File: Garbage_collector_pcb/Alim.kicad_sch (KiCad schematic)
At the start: 0 parts

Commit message: Ajout de la partie alimentation
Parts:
- added BT1: Battery_Cell, symbol Kicad:Battery_Cell
- added C12, C13: 10µF, symbol Kicad:C
- added C14, C17: 47nF, symbol Kicad:C
- added C18: 1µF, symbol Kicad:C
- added C19: 8µ2, symbol Kicad:C
- added J11: USB_C_Receptacle_USB2.0_16P, Connector_USB:USB_C_Receptacle_GCT_USB4105-xx-A_16P_TopMnt_Horizontal, symbol Kicad:USB_C_Receptacle_USB2.0_16P
- added L1: L, symbol Kicad:L
- added Q1: NMOS, symbol Kicad:NMOS
- added R10: 260, symbol Kicad:R
- added R11, R12, R13, R14, R16, R19: 10k, symbol Kicad:R
- added R15: 1k, symbol Kicad:R
- added R17: 5k23, symbol Kicad:R
- added R18: 30k1, symbol Kicad:R
- added R7, R8: 5.1k, Resistor_SMD:R_0402_1005Metric_Pad0.72x0.64mm_HandSolder, symbol Device:R
- added SW1: SW_Push, symbol Kicad:SW_Push
- added U2: BQ25896RTWR, Package_DFN_QFN:Texas_RTW_WQFN-24-1EP_4x4mm_P0.5mm_EP2.7x2.7mm, symbol Ext_library:BQ25896RTWR
- added U4: USBLC6-2P6, Package_TO_SOT_SMD:SOT-23-6, symbol Power_Protection:USBLC6-2P6
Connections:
- new net: R10.2, U2.10 (ILIM)
- new net: R17.2, R18.1, R19.1, U2.11 (TS)
- new net: SW1.1, U2.12 (~{QON})
- new net: BT1.1 (+), U2.13 (BAT), U2.14 (BAT)
- new net: C14.2, L1.1, U2.19 (SW), U2.20 (SW)
- new net: C12.1, C13.1, C14.1, U2.21 (BTST)
- new net: C19.2, U2.23 (PMID)
- new net: J11.A5 (CC1), R7.1
- new net: J11.B5 (CC2), R8.2
- new net: Q1.2 (G), R14.2, R15.2
- new net +3.3V: R11.1, R12.2, R13.1
- new net D+: J11.A6 (D+), J11.B6 (D+), U4.3 (I/O2)
- new net D-: J11.A7 (D-), J11.B7 (D-), U4.1 (I/O1)
- new net DP+: U4.4 (I/O2)
- new net DP-: U4.6 (I/O1)
- new net EXP: BT1.2 (-), C17.1, C18.1, C19.1, J11.A1 (GND), J11.A12 (GND), J11.B1 (GND), J11.B12 (GND), J11.SH (SHIELD), Q1.3 (S), R10.1, R14.1, R18.2, R19.2, R7.2, R8.1, SW1.2, U2.17 (PGND), U2.18 (PGND), U2.2 (PSEL), U2.25 (EXP), U2.9 (~{CE}), U4.2 (GND)
- new net INT: R11.2, U2.7 (INT)
- new net OTG: Q1.1 (D), R16.1, U2.8 (OTG)
- new net REGN: C17.2, R17.1, U2.22 (REGN)
- new net SCL: U2.5 (SCL)
- new net SDA: U2.6 (SDA)
- new net STAT: R12.1, U2.4 (STAT)
- new net SYS: C12.2, C13.2, L1.2, R16.2, U2.15 (SYS), U2.16 (SYS)
- new net VBUS: C18.2, J11.A4 (VBUS), J11.A9 (VBUS), J11.B4 (VBUS), J11.B9 (VBUS), R15.1, U2.1 (VBUS), U4.5 (VBUS)
- new net ~{PG}: R13.2, U2.3 (~{PG})
- no-connect marks 0 -> 2
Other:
- note added: "Activation du boost interne (Si USB absent)"
- note added: "Chargeur"
- note added: "Connecteur USB C"
- note added: "Protection ESD"
- note added: "Resistances de tirage"

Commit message: update alim part
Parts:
- removed J11: USB_C_Receptacle_USB2.0_16P, Connector_USB:USB_C_Receptacle_GCT_USB4105-xx-A_16P_TopMnt_Horizontal, symbol Kicad:USB_C_Receptacle_USB2.0_16P
- removed U4: USBLC6-2P6, Package_TO_SOT_SMD:SOT-23-6, symbol Power_Protection:USBLC6-2P6
- added C20, C21: 10µ, symbol Kicad:C
- added C22: 470nF, symbol Kicad:C
- added C23: 2µ2, symbol Kicad:C
- added J12: USB_C_Receptacle_PowerOnly_6P, symbol Kicad:USB_C_Receptacle_PowerOnly_6P
- added PS1: BU33SD5WG-TR, BU33SD5WG-TR:SOT95P280X125-5N, symbol Kicad:BU33SD5WG-TR
- added R20, R21: 10k, symbol Kicad:R
- added R9: 10m, Resistor_SMD:R_0402_1005Metric_Pad0.72x0.64mm_HandSolder, symbol Device:R
- added U4: BQ27220YZFR, YZF9_TEX, symbol Ext_library:BQ27220YZFR
- C17: value 47nF -> 4µ7
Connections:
- net +3.3V: now also R20.1
- net EXP: now also C12.1, C13.1, C20.1, C21.1, C22.1, C23.1, J12.A12 (GND), J12.B12 (GND), J12.SH (SHIELD), PS1.2 (GND), R21.2, U4.B2 (VSS)
- net VBUS: now also J12.A9 (VBUS), J12.B9 (VBUS), PS1.1 (VIN), PS1.3 (STBY)
- net +BATT: now reaches U2.13 (BAT), U2.14 (BAT)
- net +BATT: now also R9.1, U4.C2 (SRN); no longer BT1.1 (+)
- net at C14.1, U2.21 (BTST): no longer C12.1, C13.1
- net at R7.1: now also J12.A5 (CC1)
- net at R8.2: now also J12.B5 (CC2)
- new net: R21.1, U4.B1 (VIN)
- new net: R20.2, U4.A1 (GPOUT)
- new net: C22.2, C23.2, U4.B3 (VDD)
- new net: C21.2, PS1.5 (VOUT)
- new net BAT+: BT1.1 (+), R9.2, U4.C1 (SRP)
- no-connect marks 2 -> 0
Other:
- note removed: "Protection ESD"
- moved on the sheet: Q1, R11, R12, R13, R14, R15, R16, R7, R8

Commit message: update alim part
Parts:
- added C24: 1µF, symbol Kicad:C
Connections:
- net SCL is gone; now on net I2C1_SCL: U2.5 (SCL)
- net SDA is gone; now on net I2C1_SDA: U2.6 (SDA)
- net EXP: now also C24.1
- net I2C1_SDA: now reaches U4.A2 (SDA)
- net I2C1_SCL: now reaches U4.A3 (SCL)
- net BAT+ renamed bat
- net bat: now also U4.C3 (BAT), C24.2
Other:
- note added: "Batterie - Lipo 1S 3400mAh"
- moved on the sheet: BT1, C12, C13, C14, C17, C18, C19, C22, C23, L1, Q1, R10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

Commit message: seance 24 septembre
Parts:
- added D3: D, symbol Kicad:D
- added Q4: MMDT5401, Package_TO_SOT_SMD:SOT-363_SC-70-6, symbol Kicad:MMDT5401
- added Q5: PMOS, symbol Kicad:PMOS
- added R22, R23: 100k, symbol Kicad:R
- PS1: footprint BU33SD5WG-TR:SOT95P280X125-5N -> Package_SO:TSOP-5_1.65x3.05mm_P0.95mm
- U4: footprint YZF9_TEX -> Package_BGA:Texas_DSBGA-9_1.4715x1.4715mm_Layout3x3_P0.5mm
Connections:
- net +3.3V: now also C21.2, PS1.5 (VOUT)
- net +BATT: now also C20.2, PS1.1 (VIN), PS1.3 (STBY)
- net EXP: now also R22.1, R23.1
- net VBUS: now also D3.1 (K), Q4.4 (E2), Q5.1 (D); no longer PS1.1 (VIN), PS1.3 (STBY)
- net GPOUT: now reaches R20.2, U4.A1 (GPOUT)
- net I2C1_SCL renamed I2C3_SCL
- net I2C1_SDA renamed I2C3_SDA
- new net: D3.2 (A), Q4.2 (B1), Q4.3 (C2), Q4.5 (B2), R22.2
- new net: Q4.6 (C1), Q5.2 (G), R23.2
- new net USB_5V: Q4.1 (E1), Q5.3 (S)
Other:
- note added: "Fuel Gauge"

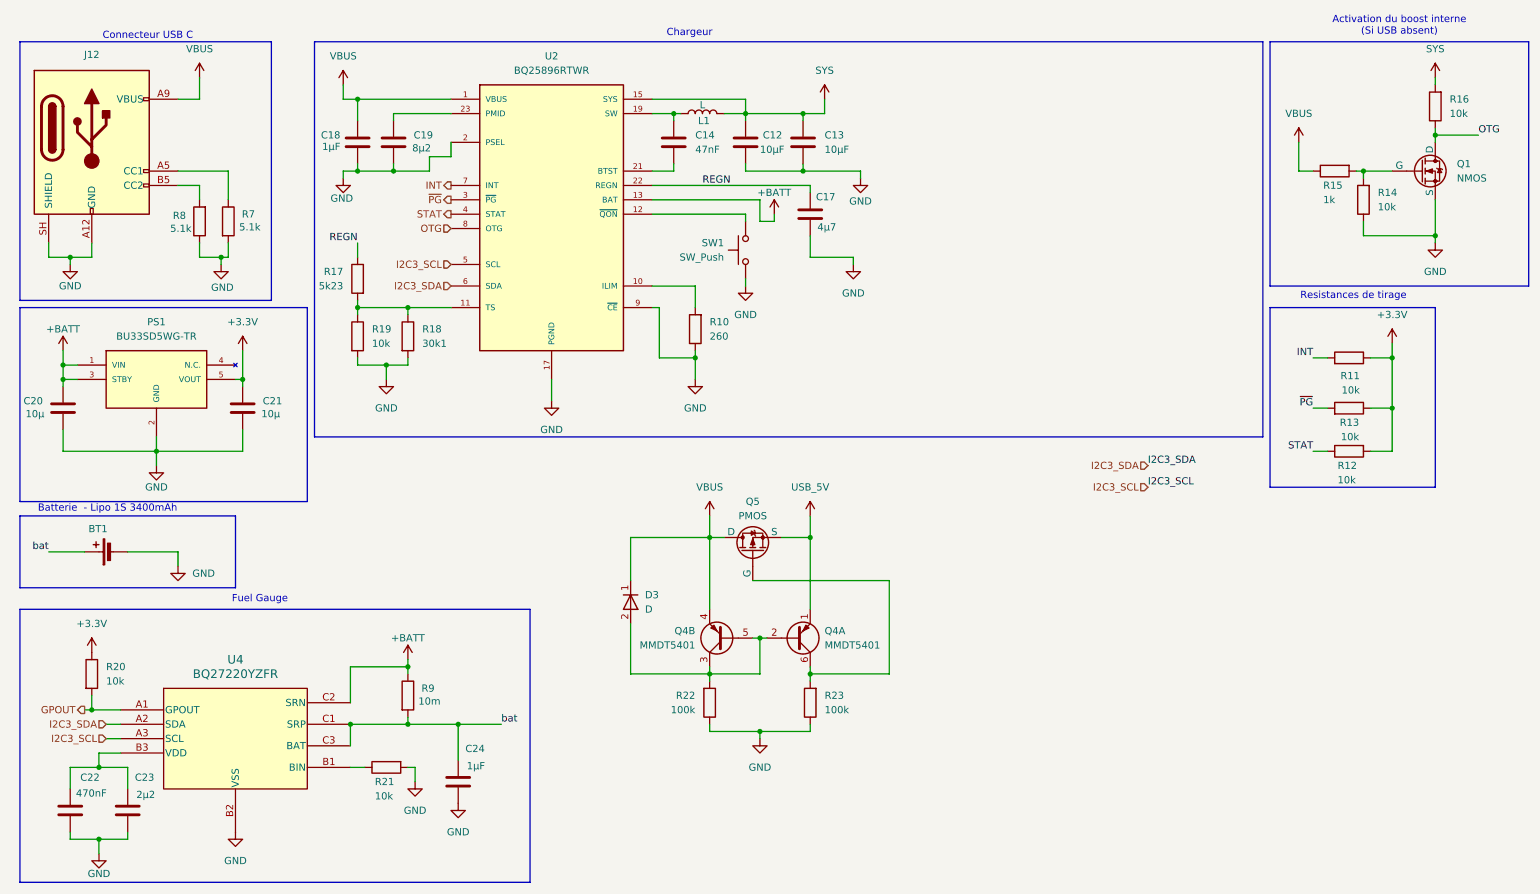
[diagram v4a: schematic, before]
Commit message: update schematic
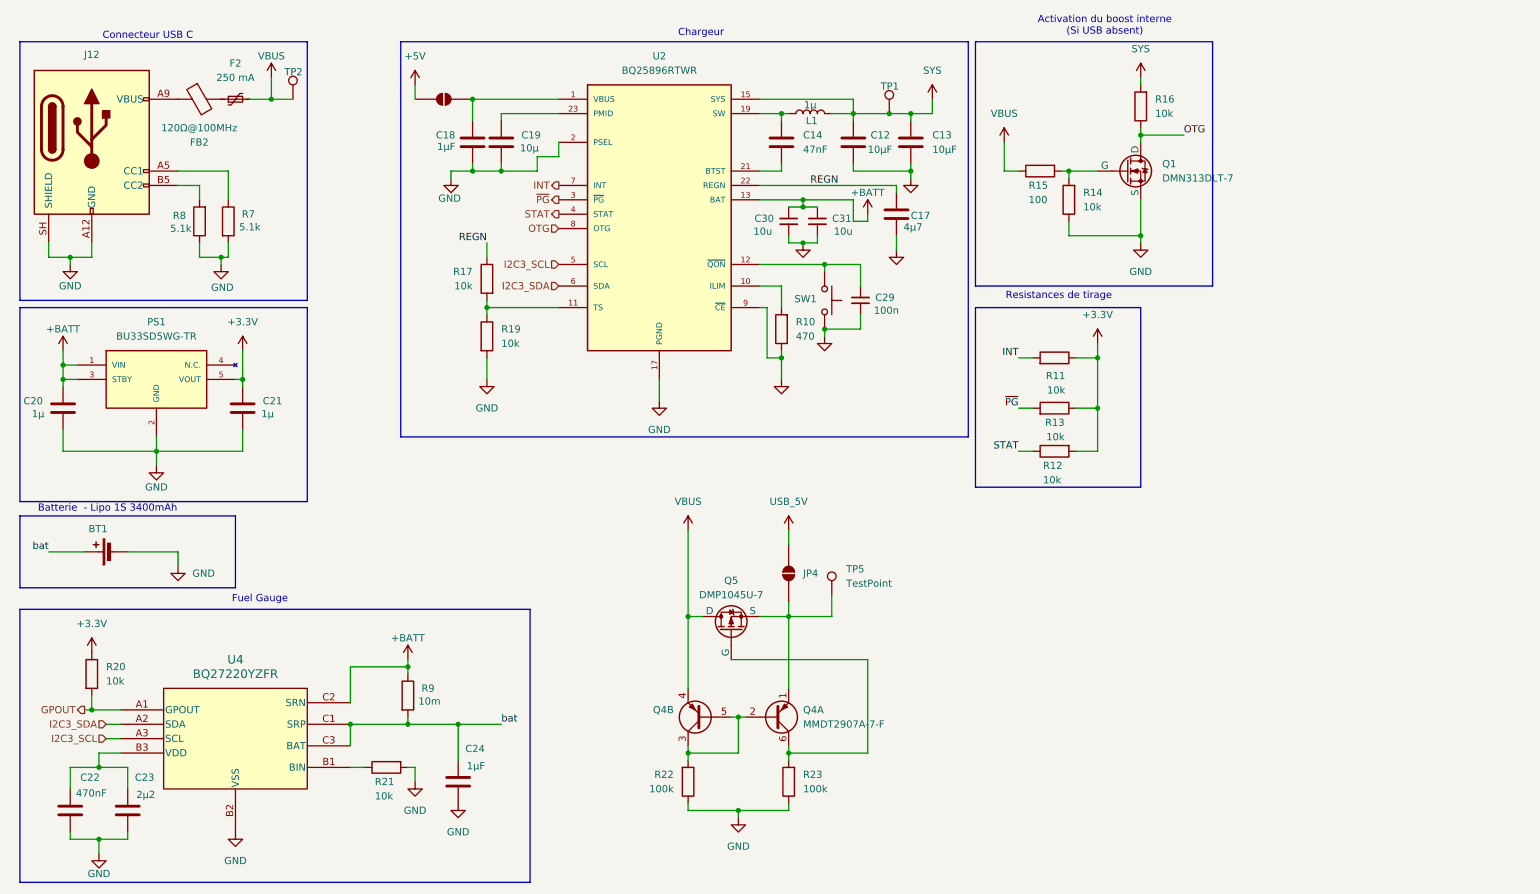
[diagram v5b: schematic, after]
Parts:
- removed D3: D, symbol Kicad:D
- removed R18: 30k1, symbol Kicad:R
- added C29: 100n, Capacitor_SMD:C_0402_1005Metric, symbol Device:C_Small
- added C30, C31: 10u, Capacitor_SMD:C_0402_1005Metric, symbol Device:C_Small
- added F2: 250 mA, Fuse:Fuse_0603_1608Metric, symbol Device:Polyfuse_Small
- added FB2: 120Ω@100MHz, Inductor_SMD:L_0603_1608Metric, symbol Device:FerriteBead
- added JP3, JP4: SolderJumper_2_Open, Jumper:SolderJumper-2_P1.3mm_Open_TrianglePad1.0x1.5mm, symbol Jumper:SolderJumper_2_Open
- added TP1, TP2, TP5: TestPoint, TestPoint:TestPoint_Pad_D2.0mm, symbol Connector:TestPoint
- C19: value 8µ2 -> 10µ
- C20, C21: value 10µ -> 1µ
- L1: value L -> 1µ
- Q1: value NMOS -> DMN313DLT-7
- Q4: value MMDT5401 -> MMDT2907A-7-F
- Q5: value PMOS -> DMP1045U-7; footprint (none) -> Package_TO_SOT_SMD:SOT-23
- R10: value 260 -> 470
- R15: value 1k -> 100
- R17: value 5k23 -> 10k
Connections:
- net +BATT: now also C30.1, C31.1
- net EXP: now also C29.2, C30.2, C31.2
- net SYS: now also TP1.1
- net USB_5V: now also JP4.2 (B); no longer Q4.1 (E1), Q5.3 (S)
- net VBUS: now also F2.2, TP2.1; no longer C18.2, J12.A9 (VBUS), J12.B9 (VBUS), U2.1 (VBUS)
- net at SW1.1, U2.12 (~{QON}): now also C29.1
- new net: F2.1, FB2.2
- new net: JP4.1 (A), Q4.1 (E1), Q5.3 (S), TP5.1
- new net: C18.2, JP3.2 (B), U2.1 (VBUS)
- new net: FB2.1, J12.A9 (VBUS), J12.B9 (VBUS)
- new net +5V: JP3.1 (A)
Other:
- moved on the sheet: C12, C13, C14, C17, C18, C19, L1, Q1, Q4A, Q4B, Q5, R10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

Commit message: ajout led temoin
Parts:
- added D3, D4, D5, D6: LED, symbol Kicad:LED
- added R24, R25: 1k5, Resistor_SMD:R_0402_1005Metric, symbol Device:R
- added R27, R28, R29, R30: 100k, symbol Kicad:R
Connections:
- net +3.3V: now also R24.1, R25.1, R27.2
- net +5V: now also R28.2
- net EXP: now also D3.1 (K), D4.1 (K)
- net I2C3_SCL: now also R25.2
- net I2C3_SDA: now also R24.2
- net STAT: now also D5.1 (K)
- net SYS: now also R29.2, R30.2
- net ~{PG}: now also D6.1 (K)
- new net: D4.2 (A), R28.1
- new net: D5.2 (A), R29.1
- new net: D6.2 (A), R30.1
- new net: D3.2 (A), R27.1

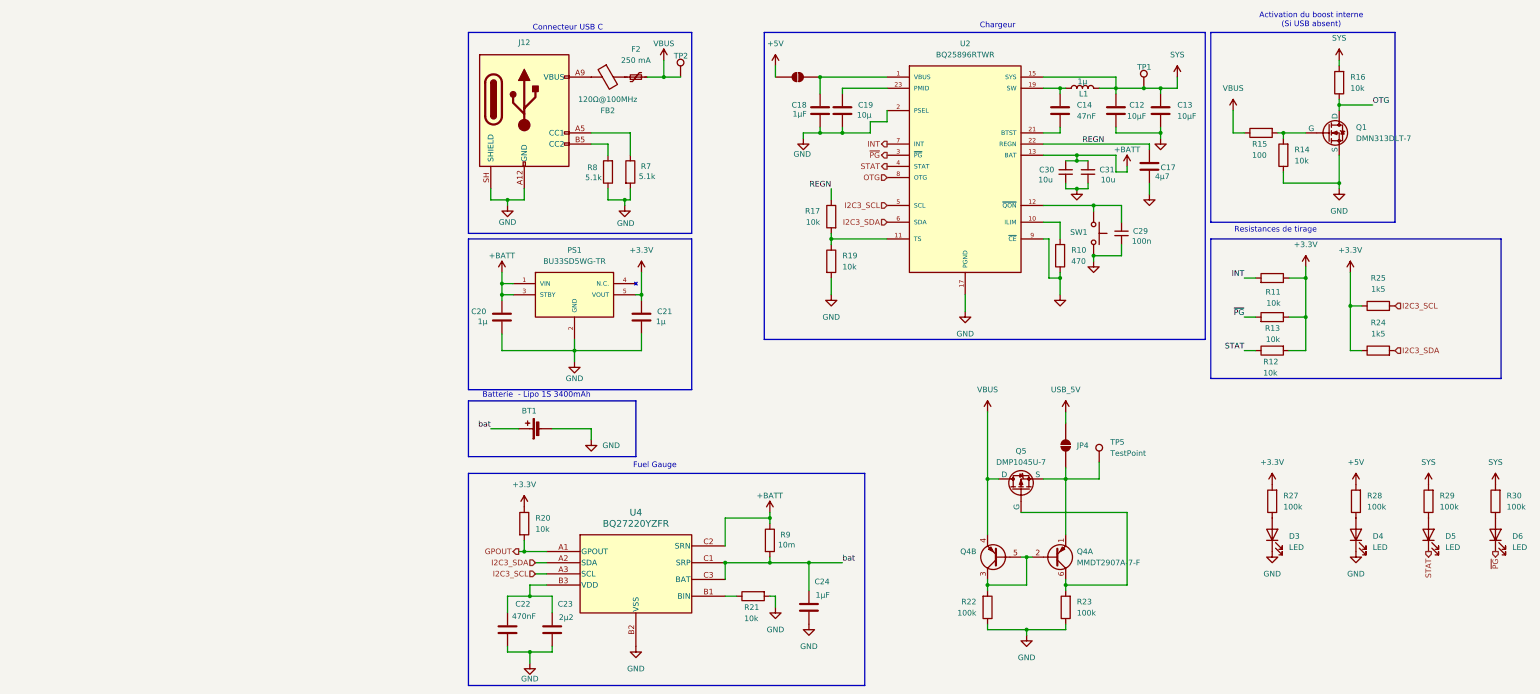
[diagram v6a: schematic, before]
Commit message: update schematic
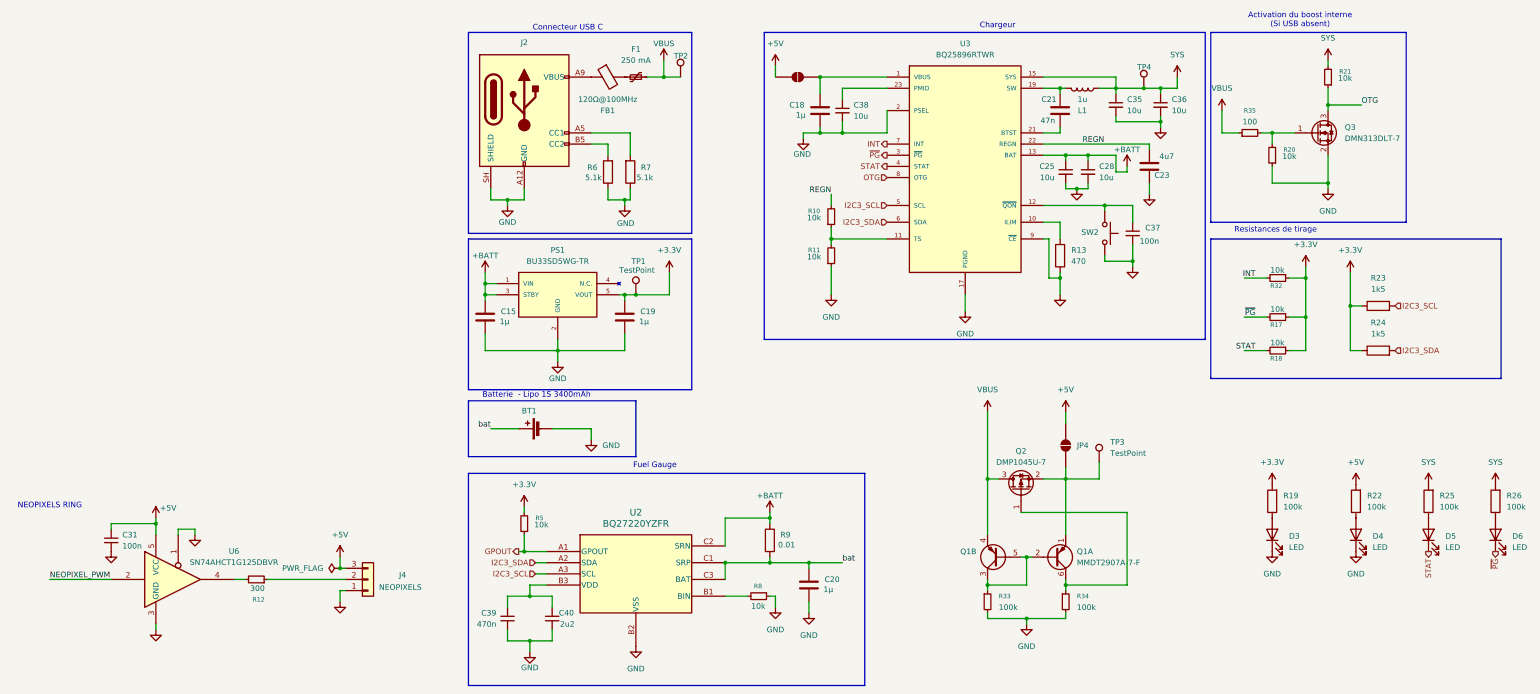
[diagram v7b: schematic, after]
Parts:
- removed C12, C13: 10µF, symbol Kicad:C
- removed C14: 47nF, symbol Kicad:C
- removed C17: 4µ7, symbol Kicad:C
- removed C21: 1µ, symbol Kicad:C
- removed C22: 470nF, symbol Kicad:C
- removed C23: 2µ2, symbol Kicad:C
- removed C24: 1µF, symbol Kicad:C
- removed C29: 100n, Capacitor_SMD:C_0402_1005Metric, symbol Device:C_Small
- removed C30: 10u, Capacitor_SMD:C_0402_1005Metric, symbol Device:C_Small
- removed L1: 1µ, symbol Kicad:L
- removed Q1: DMN313DLT-7, symbol Kicad:NMOS
- removed Q5: DMP1045U-7, Package_TO_SOT_SMD:SOT-23, symbol Kicad:PMOS
- removed R11, R12, R13, R14, R16, R17, R19, R20, R21: 10k, symbol Kicad:R
- removed R15: 100, symbol Kicad:R
- removed R22, R23: 100k, symbol Kicad:R
- added C20: 1µ, symbol Kicad:C
- added C21: 47n, Capacitor_SMD:C_0402_1005Metric, symbol Device:C
- added C23: 4u7, Capacitor_SMD:C_0402_1005Metric, symbol Device:C
- added C25, C28, C35, C36, C38: 10u, symbol Kicad:C_Small
- added C37: 100n, Capacitor_SMD:C_0402_1005Metric, symbol Device:C_Small
- added C39: 470n, Capacitor_SMD:C_0402_1005Metric, symbol Device:C_Small
- added C40: 2u2, Capacitor_SMD:C_0402_1005Metric, symbol Device:C_Small
- added J4: NEOPIXELS, Connector_JST:JST_GH_SM03B-GHS-TB_1x03-1MP_P1.25mm_Horizontal, symbol Connector_Generic:Conn_01x03
- added L1: 1u, Inductor_SMD:L_1008_2520Metric, symbol Device:L
- added Q2: DMP1045U-7, Package_TO_SOT_SMD:SOT-23, symbol Transistor_FET:DMP3099L
- added Q3: DMN313DLT-7, Package_TO_SOT_SMD:SOT-523, symbol Transistor_FET:DMN3150L
- added R10, R11, R17, R18, R20, R21, R32, R5, R8: 10k, Resistor_SMD:R_0402_1005Metric, symbol Device:R_Small
- added R12: 300, Resistor_SMD:R_0603_1608Metric, symbol Device:R_Small
- added R33, R34: 100k, Resistor_SMD:R_0402_1005Metric, symbol Device:R_Small
- added R35: 100, Resistor_SMD:R_0402_1005Metric, symbol Device:R_Small
- added TP1: TestPoint, TestPoint:TestPoint_Pad_D2.0mm, symbol Connector:TestPoint
- added U6: SN74AHCT1G125DBVR, Package_TO_SOT_SMD:SOT-23-5, symbol 74xGxx:74AHCT1G125
- BT1: JLCPCB Part # (none) -> C54769875
- C15: renamed from C20; JLCPCB Part # (none) -> C29266
- C18: value 1µF -> 1µ; JLCPCB Part # (none) -> C29266
- C19: value 10µ -> 1µ; JLCPCB Part # (none) -> C29266
- C31: value 10u -> 100n
- J2: renamed from J12; JLCPCB Part # (none) -> C2927026
- PS1: Availability In Stock -> (none); Check_prices https://www.snapeda.com/parts/BU33SD5WG-TR/Rohm/view-part/?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 -> (none); Description_1 Linear Voltage Regulator IC Positive Fixed 1 Output 500mA 5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 -> (none); HEIGHT 1.25mm -> (none); JLCPCB Part # (none) -> C3750265; MANUFACTURER_NAME ROHM Semiconductor -> (none); MANUFACTURER_PART_NUMBER BU33SD5WG-TR -> (none); MF Rohm -> (none); MOUSER_PART_NUMBER 755-BU33SD5WG-TR -> (none); MOUSER_PRICE-STOCK https://www.mouser.co.uk/ProductDetail/ROHM-Semiconductor/B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 -> (none); MP BU33SD5WG-TR -> (none); Package SSOP-5 Rohm -> (none); Price None -> (none); SnapEDA_Link https://www.snapeda.com/parts/BU33SD5WG-TR/Rohm/view-part/?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 -> (none)
- Q1: renamed from Q4; JLCPCB Part # (none) -> C460232
- R13: renamed from R10; JLCPCB Part # (none) -> C25117
- R6: renamed from R8; JLCPCB Part # (none) -> C25905
- R7: JLCPCB Part # (none) -> C25905
- R9: value 10m -> 0.01; footprint Resistor_SMD:R_0402_1005Metric_Pad0.72x0.64mm_HandSolder -> Resistor_SMD:R_2512_6332Metric; JLCPCB Part # (none) -> C105142
- SW2: renamed from SW1; JLCPCB Part# (none) -> C72443
- U2: renamed from U4; JLCPCB Part # (none) -> C528617
- U3: renamed from U2; Availability In Stock -> (none); CREATOR NEZY -> (none); Check_prices https://www.snapeda.com/parts/BQ25896RTWR/Texas+Instruments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 -> (none); JLCPCB Part # (none) -> C181475; MANUFACTURER Texas Instruments -> (none); MAXIMUM_PACKAGE_HEIGHT 0.80mm -> (none); MF Texas Instruments -> (none); MP BQ25896RTWR -> (none); PARTREV C -> (none); Package WQFN-24 Texas Instruments -> (none); Price None -> (none); STANDARD Manufacturer Recommendations -> (none); SnapEDA_Link https://www.snapeda.com/parts/BQ25896RTWR/Texas+Instruments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 -> (none)
- renumbered F2 to F1, FB2 to FB1, R27 to R19, R28 to R22, R25 to R23, R29 to R25, R30 to R26, TP5 to TP3, TP1 to TP4
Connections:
- net USB_5V is gone; now on net +5V: JP4.2 (B)
- net +3.3V: now also C19.2, R17.1, R18.1, R32.1, R5.2, TP1.1
- net +5V: now also C31.1, J4.3 (Pin_3), U6.5 (VCC)
- net +BATT: now also C25.1, C28.1; no longer C31.1
- net EXP: now also R7.1, C20.1, C23.1, C25.2, C28.2, C35.2, C36.2, C37.1, C38.2, C39.2, C40.2, J4.1 (Pin_1), Q3.2 (S), R11.1, R20.1, R33.2, R34.2, R8.1, U6.1, U6.3 (GND); no longer R7.2
- net GPOUT: now also R5.1
- net INT: now also R32.2
- net OTG: now also Q3.3 (D), R21.1
- net REGN: now also C23.2, R10.2
- net STAT: now also R18.2
- net SYS: now also C35.1, C36.1, L1.1, R21.2
- net VBUS: now also Q2.3 (D), R35.1
- net bat: now also C20.2
- net ~{PG}: now also R17.2
- net at JP4.1 (A), Q1.1 (E1), TP3.1: now also Q2.2 (S)
- net at Q1.2 (B1), Q1.3 (C2), Q1.5 (B2): now also R33.1
- net at Q1.6 (C1): now also Q2.1 (G), R34.1
- net at U3.11 (TS): now also R10.1, R11.2
- net at SW2.1, U3.12 (~{QON}): now also C37.2
- net at U3.19 (SW), U3.20 (SW): now also C21.2, L1.2
- net at U3.21 (BTST): now also C21.1
- net at U3.23 (PMID): now also C38.1; no longer C19.2
- net at U2.B1 (BIN): now also R8.2
- net at J2.A5 (CC1): now also R7.2; no longer R7.1
- net at U2.B3 (VDD): now also C39.1, C40.1
- new net: J4.2 (Pin_2), R12.1
- new net: Q3.1 (G), R20.2, R35.2
- new net: R12.2, U6.4
- new net NEOPIXEL_PWM: U6.2
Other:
- note added: "NEOPIXELS RING"
- moved on the sheet: C15, PS1, SW2
